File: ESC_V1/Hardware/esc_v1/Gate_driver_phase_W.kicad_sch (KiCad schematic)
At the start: 9 parts, among them U8 UCC27282DR

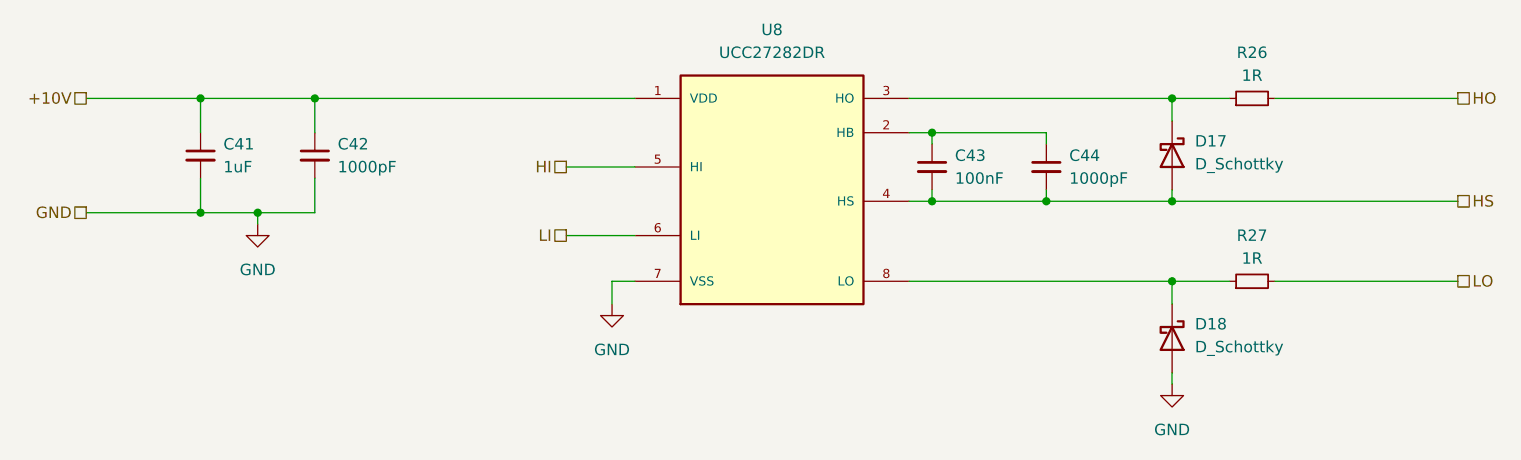
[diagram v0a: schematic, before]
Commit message: Components roughly placed in layout
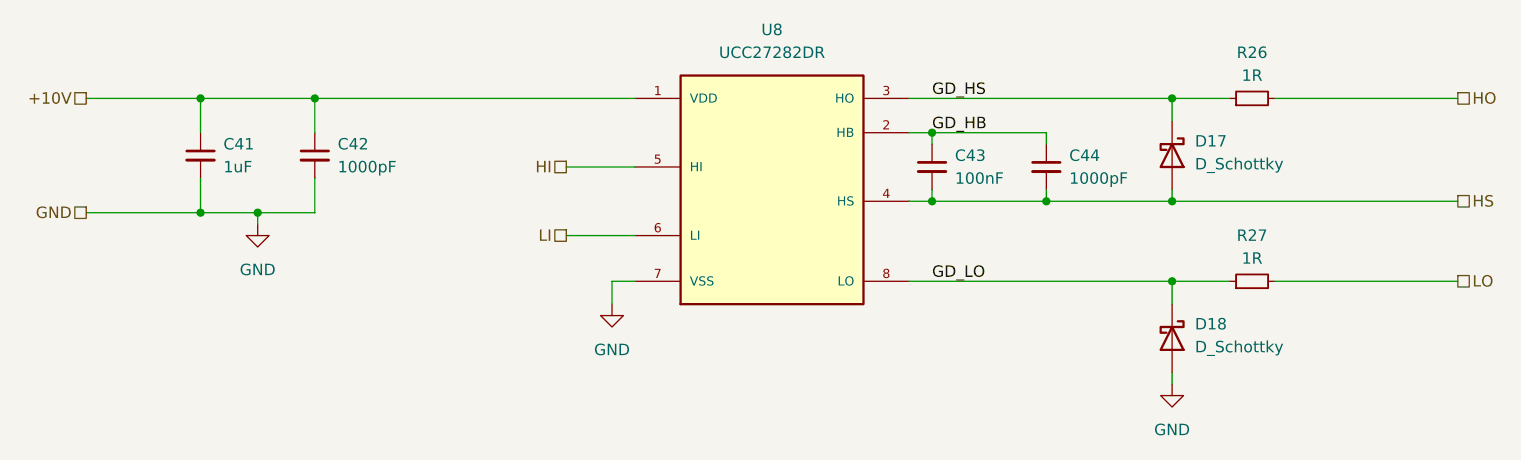
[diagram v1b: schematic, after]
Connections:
- net GD_HB: now reaches C43.1, C44.1, U8.2 (HB)
- net GD_HS: now reaches D17.1 (K), R26.1, U8.3 (HO)
- net GD_LO: now reaches D18.1 (K), R27.1, U8.8 (LO)
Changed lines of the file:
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@@
     (stroke (width 0) (type default) (color 0 0 0 0))
+  )
+  (label "GD_LO" (at 157.48 109.22 0)
+    (effects (font (size 1.27 1.27)) (justify left bottom))
+  )
+  (label "GD_HS" (at 157.48 88.9 0)
+    (effects (font (size 1.27 1.27)) (justify left bottom))
+  )
+  (label "GD_HB" (at 157.48 92.71 0)
+    (effects (font (size 1.27 1.27)) (justify left bottom))
   )
   (hierarchical_label "LO" (shape passive) (at 215.9 109.22 0)
